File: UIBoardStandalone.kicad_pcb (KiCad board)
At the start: 2 copper layers, 132 x 68.5 mm, 49 parts, among them J10 Conn_02x15_Odd_Even, J17 Conn_02x08_Odd_Even, SW1 Button_X, SW10 Button_6, SW11 Button_S, SW12 Button_7, SW13 Button_8, SW14 Button_9, SW15 Button_G, SW16 Button_Y, SW17 Button_0, SW18 Button_Z, SW2 Button_R, SW3 Button_1, SW4 Button_2, SW5 Button_3, SW6 Button_P, SW7 Button_M, SW8 Button_4, SW9 Button_5, U1 HD1077R, U10 MM74C923, U11 HD1077R, U12 HD1077R, U13 HD1077R, U14 HD1077R, U15 HD1077R, U16 HD1077R, U17 HD1077R, U2 HD1077R, U3 HD1077R, U4 HD1077R, U5 HD1077R, U6 HD1077R, U7 HD1077R, U8 HD1077R, U9 HD1077R

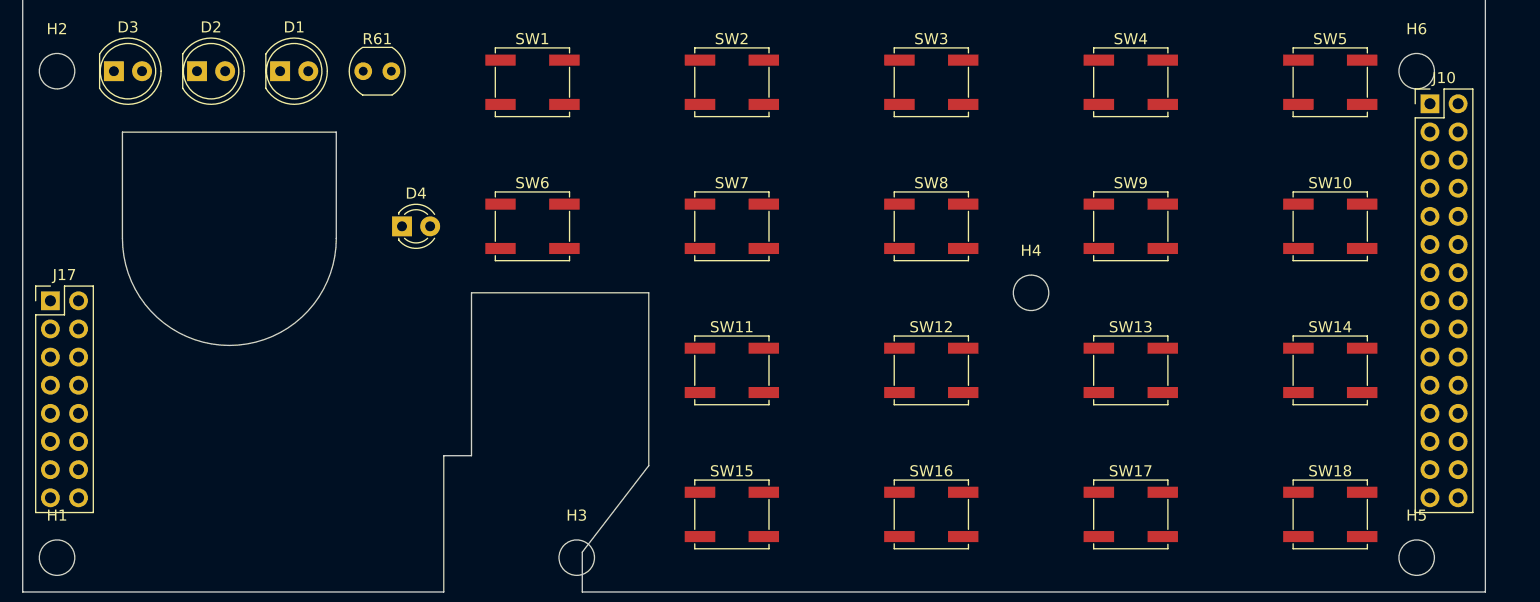
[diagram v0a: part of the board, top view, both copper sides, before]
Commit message: - Steckverbinder auf Rueckseite gespiegelt
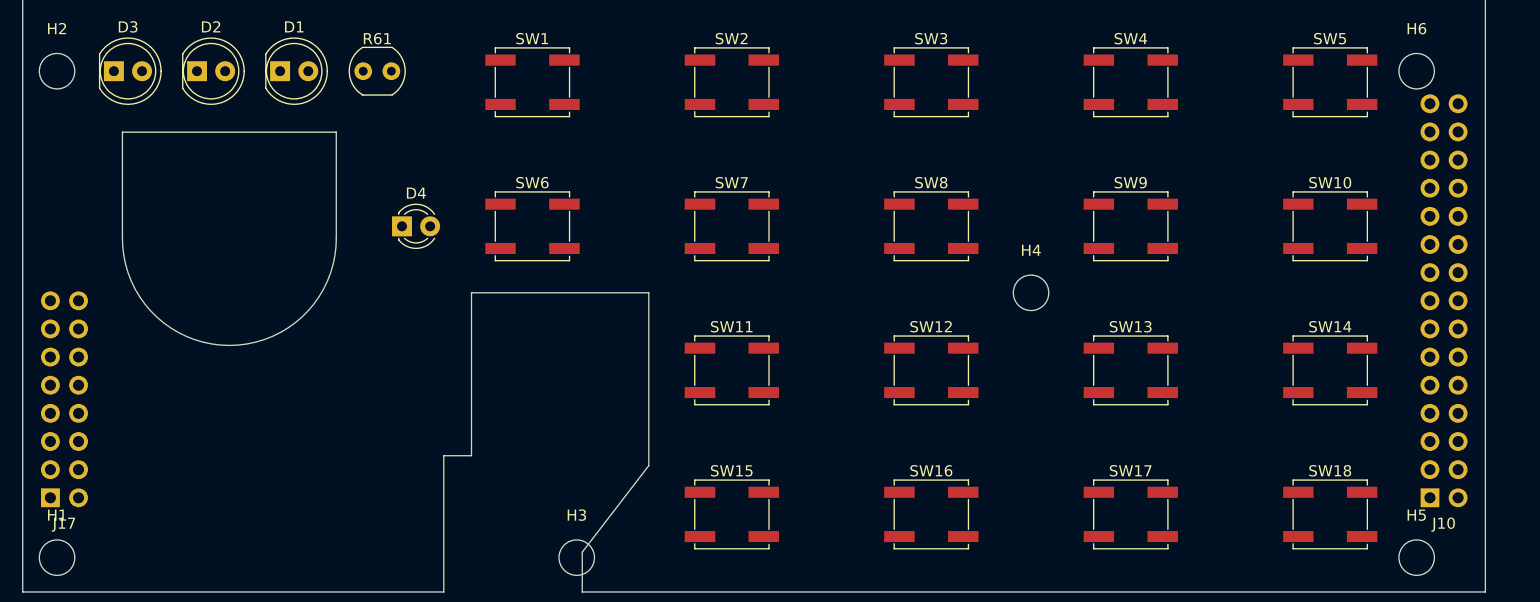
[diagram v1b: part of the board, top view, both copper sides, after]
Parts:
- J10, J17: moved to B.Cu
- moved J10 35.6 mm to (127.0, 60.0)
- moved J17 17.8 mm to (2.50, 60.0)

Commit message: - Outline / Postionierung Zwischenstand
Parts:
- moved U2 125.4 mm to (92.6, 69.0)
- moved U3 125.2 mm to (100.2, 69.0)
- moved U4 124.9 mm to (107.9, 69.0)
- moved U5 124.7 mm to (115.5, 69.0)
- moved U6 124.4 mm to (123.1, 69.0)
- moved U7 124.2 mm to (130.7, 69.0)
- moved U8 123.9 mm to (138.3, 69.0)
- moved U9 123.7 mm to (146.0, 69.0)
- moved U10 123.4 mm to (153.6, 69.0)
- moved U11 123.2 mm to (161.2, 69.0)
- moved U12 122.9 mm to (168.8, 69.0)
- moved U13 122.7 mm to (176.4, 69.0)
- moved U14 122.4 mm to (184.1, 69.0)
- moved U15 122.2 mm to (191.7, 69.0)
- moved H5 100.0 mm to (207.5, 123.0)
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- renumbered J17 to J1, J10 to J2, R61 to R1, U11 to U10, U12 to U11, U13 to U12, U14 to U13, U15 to U14, U16 to U15, U17 to U16, U10 to U17

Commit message: - erster Stand für Abmessungen
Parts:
- D1: value LED_RED -> LED_RD
- D2: value LED_YELLOW -> LED_YL
- D3: value LED_GREEN -> LED_GN
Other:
- board text added: "Ø3,2"
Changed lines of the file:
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@@
   (general
     (thickness 1.6)
-    (drawings 60)
+    (drawings 66)
     (tracks 0)
     (zones 0)
@@
       (effects (font (size 1 1) (thickness 0.15)))
     )
-    (fp_text value LED_GREEN (at 5.5 0 180) (layer F.Fab)
+    (fp_text value LED_GN (at 5.5 0 180) (layer F.Fab)
       (effects (font (size 1 1) (thickness 0.15)))
     )
@@
       (effects (font (size 1 1) (thickness 0.15)))
     )
-    (fp_text value LED_YELLOW (at 5.5 0 180) (layer F.Fab)
+    (fp_text value LED_YL (at 5.5 0 180) (layer F.Fab)
       (effects (font (size 1 1) (thickness 0.15)))
     )
@@
       (effects (font (size 1 1) (thickness 0.15)))
     )
-    (fp_text value LED_RED (at 5.5 0 180) (layer F.Fab)
+    (fp_text value LED_RD (at 5.5 0 180) (layer F.Fab)
       (effects (font (size 1 1) (thickness 0.15)))
     )
@@
     )
   )
+  (gr_text Ø3,2 (at 86 73.5) (layer Dwgs.User)
+    (effects (font (size 1 1) (thickness 0.15)))
+  )
+  (gr_text Ø3,2 (at 169.5 95) (layer Dwgs.User)
+    (effects (font (size 1 1) (thickness 0.15)))
+  )
+  (gr_text Ø3,2 (at 203 73.5) (layer Dwgs.User)
+    (effects (font (size 1 1) (thickness 0.15)))
+  )
+  (gr_text Ø3,2 (at 203 120.5) (layer Dwgs.User)
+    (effects (font (size 1 1) (thickness 0.15)))
+  )
+  (gr_text Ø3,2 (at 129 119) (layer Dwgs.User)
+    (effects (font (size 1 1) (thickness 0.15)))
+  )
+  (gr_text Ø3,2 (at 86 120.5) (layer Dwgs.User)
+    (effects (font (size 1 1) (thickness 0.15)))
+  )
   (dimension 3 (width 0.15) (layer Dwgs.User)
     (gr_text "3,0 mm" (at 74.2 124.5 90) (layer Dwgs.User)
@@
   )
   (dimension 53.000094 (width 0.15) (layer Dwgs.User)
-    (gr_text "53,000 mm" (at 105.042264 145.349995 0.1081051161) (layer Dwgs.User)
-      (effects (font (size 1 1) (thickness 0.15)))
-    )
-    (feature1 (pts (xy 78.5 123) (xy 78.540918 144.686417)))
-    (feature2 (pts (xy 131.5 122.9) (xy 131.540918 144.586417)))
-    (crossbar (pts (xy 131.539811 143.999997) (xy 78.539811 144.099997)))
-    (arrow1a (pts (xy 78.539811 144.099997) (xy 79.665206 143.511452)))
-    (arrow1b (pts (xy 78.539811 144.099997) (xy 79.667419 144.684291)))
-    (arrow2a (pts (xy 131.539811 143.999997) (xy 130.412203 143.415703)))
-    (arrow2b (pts (xy 131.539811 143.999997) (xy 130.414416 144.588542)))
+    (gr_text "53,000 mm" (at 105.042264 145.349994 0.1081051161) (layer Dwgs.User)
+      (effects (font (size 1 1) (thickness 0.15)))
+    )
+    (feature1 (pts (xy 78.5 123) (xy 78.540918 144.686416)))
+    (feature2 (pts (xy 131.5 122.9) (xy 131.540918 144.586416)))
+    (crossbar (pts (xy 131.539811 143.999996) (xy 78.539811 144.099996)))
+    (arrow1a (pts (xy 78.539811 144.099996) (xy 79.665206 143.511451)))
+    (arrow1b (pts (xy 78.539811 144.099996) (xy 79.667419 144.68429)))
+    (arrow2a (pts (xy 131.539811 143.999996) (xy 130.412203 143.415702)))
+    (arrow2b (pts (xy 131.539811 143.999996) (xy 130.414416 144.588541)))
   )
   (dimension 114.3 (width 0.15) (layer Dwgs.User)

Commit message: [fix:] measurement errors [add:] backlight LEDs
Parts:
- added D5: LED_BL1, LED_THT:LED_D3.0mm, F.Cu at (115.5, 87.3)
- added D6: LED_BL2, LED_THT:LED_D3.0mm, F.Cu at (151.5, 87.3)
- added D7: LED_BL3, LED_THT:LED_D3.0mm, F.Cu at (187.5, 87.3)
- added D8: LED_BL4, LED_THT:LED_D3.0mm, F.Cu at (151.5, 113.8)
- added D9: LED_BL5, LED_THT:LED_D3.0mm, F.Cu at (187.5, 113.8)
- moved D1 1.00 mm to (102.8, 81.3)
- moved D2 1.00 mm to (95.3, 81.3)
- moved D3 1.00 mm to (87.8, 81.3)
- moved R1 1.00 mm to (110.3, 81.3)
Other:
- outline, holes or cut-outs redrawn

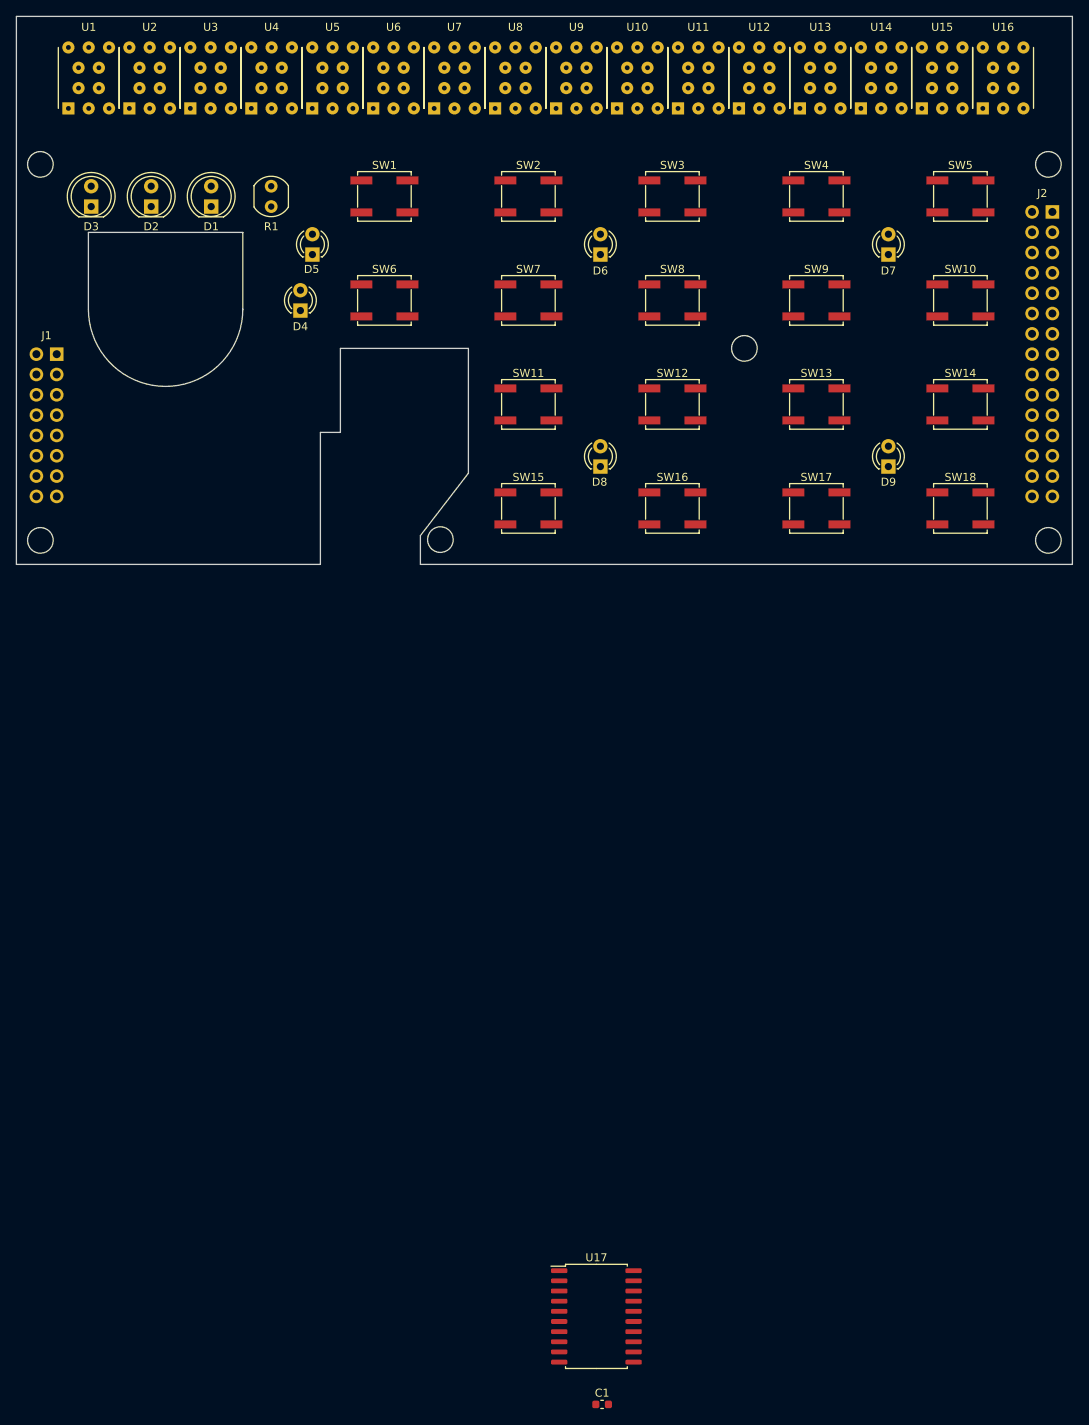
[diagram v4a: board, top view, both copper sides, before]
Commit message: - Erster Stand UI Board Layout
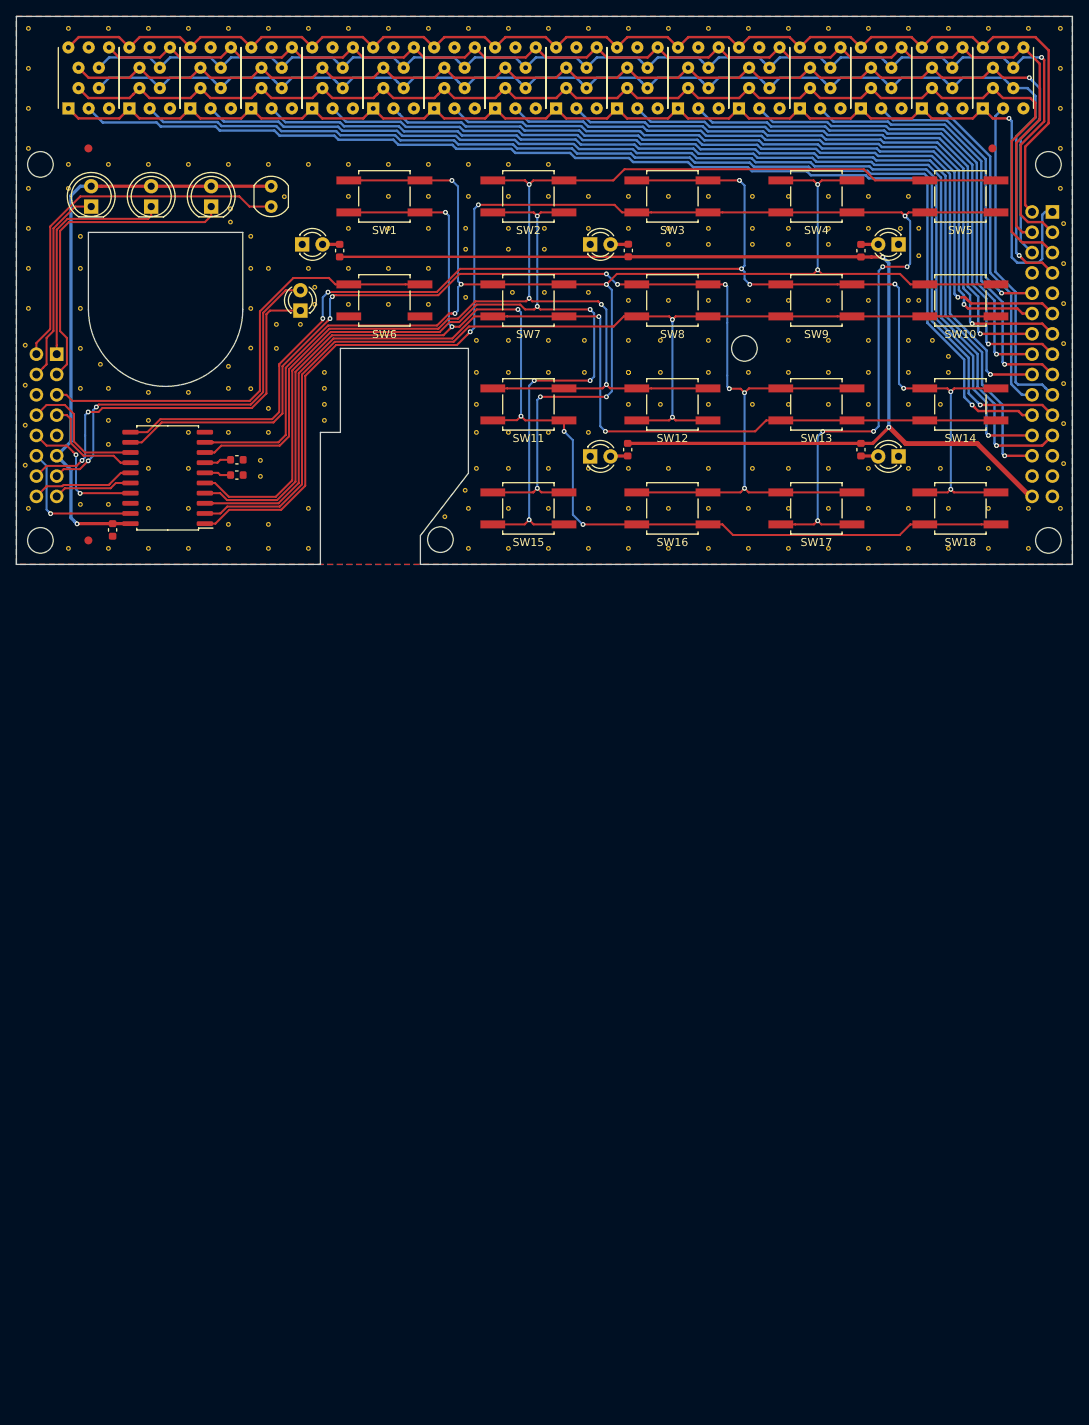
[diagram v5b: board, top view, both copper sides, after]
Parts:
- added C2: 2u2/10V/X5R, Capacitor_SMD:C_0603_1608Metric, F.Cu at (106.1, 112.9)
- added C3: 220n/10V/X5R, Capacitor_SMD:C_0603_1608Metric, F.Cu at (106.1, 114.8)
- added R2: tbd, Resistor_SMD:R_0603_1608Metric, F.Cu at (118.9, 86.8)
- added R3: tbd, Resistor_SMD:R_0603_1608Metric, F.Cu at (155.0, 86.8)
- added R4: tbd, Resistor_SMD:R_0603_1608Metric, F.Cu at (184.1, 86.8)
- added R5: tbd, Resistor_SMD:R_0603_1608Metric, F.Cu at (154.9, 111.7)
- added R6: tbd, Resistor_SMD:R_0603_1608Metric, F.Cu at (184.1, 111.7)
- added REF**: VIA_0.6mm, TeKaDe:VIA_0.6mm, F.Cu at (134.7, 84.0)
- added REF**: VIA_0.6mm, TeKaDe:VIA_0.6mm, F.Cu at (100.0, 76.0)
- added REF**: VIA_0.6mm, TeKaDe:VIA_0.6mm, F.Cu at (85.0, 76.0)
- added REF**: VIA_0.6mm, TeKaDe:VIA_0.6mm, F.Cu at (190.0, 80.0)
- added REF**: VIA_0.6mm, TeKaDe:VIA_0.6mm, F.Cu at (185.0, 80.0)
- added REF**: VIA_0.6mm, TeKaDe:VIA_0.6mm, F.Cu at (180.0, 80.0)
- added REF**: VIA_0.6mm, TeKaDe:VIA_0.6mm, F.Cu at (175.0, 80.0)
- added REF**: VIA_0.6mm, TeKaDe:VIA_0.6mm, F.Cu at (170.5, 80.0)
- added REF**: VIA_0.6mm, TeKaDe:VIA_0.6mm, F.Cu at (165.0, 80.0)
- added REF**: VIA_0.6mm, TeKaDe:VIA_0.6mm, F.Cu at (160.0, 80.0)
- added REF**: VIA_0.6mm, TeKaDe:VIA_0.6mm, F.Cu at (155.0, 80.0)
- added REF**: VIA_0.6mm, TeKaDe:VIA_0.6mm, F.Cu at (150.0, 80.0)
- added REF**: VIA_0.6mm, TeKaDe:VIA_0.6mm, F.Cu at (105.0, 76.0)
- added REF**: VIA_0.6mm, TeKaDe:VIA_0.6mm, F.Cu at (145.0, 80.0)
- added REF**: VIA_0.6mm, TeKaDe:VIA_0.6mm, F.Cu at (140.0, 80.0)
- added REF**: VIA_0.6mm, TeKaDe:VIA_0.6mm, F.Cu at (135.0, 80.0)
- added REF**: VIA_0.6mm, TeKaDe:VIA_0.6mm, F.Cu at (130.0, 80.0)
- added REF**: VIA_0.6mm, TeKaDe:VIA_0.6mm, F.Cu at (125.0, 80.0)
- added REF**: VIA_0.6mm, TeKaDe:VIA_0.6mm, F.Cu at (120.0, 80.0)
- added REF**: VIA_0.6mm, TeKaDe:VIA_0.6mm, F.Cu at (85.0, 79.0)
- added REF**: VIA_0.6mm, TeKaDe:VIA_0.6mm, F.Cu at (189.0, 84.0)
- added REF**: VIA_0.6mm, TeKaDe:VIA_0.6mm, F.Cu at (185.0, 84.0)
- added REF**: VIA_0.6mm, TeKaDe:VIA_0.6mm, F.Cu at (180.0, 84.0)
- added REF**: VIA_0.6mm, TeKaDe:VIA_0.6mm, F.Cu at (110.0, 76.0)
- added REF**: VIA_0.6mm, TeKaDe:VIA_0.6mm, F.Cu at (175.0, 84.0)
- added REF**: VIA_0.6mm, TeKaDe:VIA_0.6mm, F.Cu at (170.5, 84.0)
- added REF**: VIA_0.6mm, TeKaDe:VIA_0.6mm, F.Cu at (165.0, 84.0)
- added REF**: VIA_0.6mm, TeKaDe:VIA_0.6mm, F.Cu at (160.0, 84.0)
- added REF**: VIA_0.6mm, TeKaDe:VIA_0.6mm, F.Cu at (155.0, 84.0)
- added REF**: VIA_0.6mm, TeKaDe:VIA_0.6mm, F.Cu at (150.0, 84.0)
- added REF**: VIA_0.6mm, TeKaDe:VIA_0.6mm, F.Cu at (144.5, 84.0)
- added REF**: VIA_0.6mm, TeKaDe:VIA_0.6mm, F.Cu at (140.0, 84.0)
- added REF**: VIA_0.6mm, TeKaDe:VIA_0.6mm, F.Cu at (130.0, 84.0)
- added REF**: VIA_0.6mm, TeKaDe:VIA_0.6mm, F.Cu at (125.0, 84.0)
- added REF**: VIA_0.6mm, TeKaDe:VIA_0.6mm, F.Cu at (115.0, 76.0)
- added REF**: VIA_0.6mm, TeKaDe:VIA_0.6mm, F.Cu at (120.0, 84.0)
- added REF**: VIA_0.6mm, TeKaDe:VIA_0.6mm, F.Cu at (86.5, 85.0)
- added REF**: VIA_0.6mm, TeKaDe:VIA_0.6mm, F.Cu at (180.0, 86.0)
- added REF**: VIA_0.6mm, TeKaDe:VIA_0.6mm, F.Cu at (175.0, 86.0)
- added REF**: VIA_0.6mm, TeKaDe:VIA_0.6mm, F.Cu at (170.5, 86.0)
- added REF**: VIA_0.6mm, TeKaDe:VIA_0.6mm, F.Cu at (165.0, 86.0)
- added REF**: VIA_0.6mm, TeKaDe:VIA_0.6mm, F.Cu at (160.0, 86.0)
- added REF**: VIA_0.6mm, TeKaDe:VIA_0.6mm, F.Cu at (144.5, 86.6)
- added REF**: VIA_0.6mm, TeKaDe:VIA_0.6mm, F.Cu at (140.0, 86.6)
- added REF**: VIA_0.6mm, TeKaDe:VIA_0.6mm, F.Cu at (130.0, 89.0)
- added REF**: VIA_0.6mm, TeKaDe:VIA_0.6mm, F.Cu at (112.0, 80.0)
- added REF**: VIA_0.6mm, TeKaDe:VIA_0.6mm, F.Cu at (125.0, 89.0)
- added REF**: VIA_0.6mm, TeKaDe:VIA_0.6mm, F.Cu at (120.0, 89.0)
- added REF**: VIA_0.6mm, TeKaDe:VIA_0.6mm, F.Cu at (115.0, 89.0)
- added REF**: VIA_0.6mm, TeKaDe:VIA_0.6mm, F.Cu at (110.0, 89.0)
- added REF**: VIA_0.6mm, TeKaDe:VIA_0.6mm, F.Cu at (86.5, 89.0)
- added REF**: VIA_0.6mm, TeKaDe:VIA_0.6mm, F.Cu at (190.0, 93.0)
- added REF**: VIA_0.6mm, TeKaDe:VIA_0.6mm, F.Cu at (185.0, 93.0)
- added REF**: VIA_0.6mm, TeKaDe:VIA_0.6mm, F.Cu at (180.0, 93.0)
- added REF**: VIA_0.6mm, TeKaDe:VIA_0.6mm, F.Cu at (175.0, 93.0)
- added REF**: VIA_0.6mm, TeKaDe:VIA_0.6mm, F.Cu at (170.0, 93.0)
- added REF**: VIA_0.6mm, TeKaDe:VIA_0.6mm, F.Cu at (105.3, 83.2)
- added REF**: VIA_0.6mm, TeKaDe:VIA_0.6mm, F.Cu at (165.0, 93.0)
- added REF**: VIA_0.6mm, TeKaDe:VIA_0.6mm, F.Cu at (160.0, 93.0)
- added REF**: VIA_0.6mm, TeKaDe:VIA_0.6mm, F.Cu at (155.0, 93.0)
- added REF**: VIA_0.6mm, TeKaDe:VIA_0.6mm, F.Cu at (150.0, 92.0)
- added REF**: VIA_0.6mm, TeKaDe:VIA_0.6mm, F.Cu at (140.5, 92.0)
- added REF**: VIA_0.6mm, TeKaDe:VIA_0.6mm, F.Cu at (130.0, 93.5)
- added REF**: VIA_0.6mm, TeKaDe:VIA_0.6mm, F.Cu at (125.0, 93.5)
- added REF**: VIA_0.6mm, TeKaDe:VIA_0.6mm, F.Cu at (120.0, 93.5)
- added REF**: VIA_0.6mm, TeKaDe:VIA_0.6mm, F.Cu at (115.8, 93.5)
- added REF**: VIA_0.6mm, TeKaDe:VIA_0.6mm, F.Cu at (86.5, 94.0)
- added REF**: VIA_0.6mm, TeKaDe:VIA_0.6mm, F.Cu at (105.3, 81.6)
- added REF**: VIA_0.6mm, TeKaDe:VIA_0.6mm, F.Cu at (195.0, 100.0)
- added REF**: VIA_0.6mm, TeKaDe:VIA_0.6mm, F.Cu at (190.0, 98.0)
- added REF**: VIA_0.6mm, TeKaDe:VIA_0.6mm, F.Cu at (185.0, 98.0)
- added REF**: VIA_0.6mm, TeKaDe:VIA_0.6mm, F.Cu at (180.0, 98.0)
- added REF**: VIA_0.6mm, TeKaDe:VIA_0.6mm, F.Cu at (175.0, 98.0)
- added REF**: VIA_0.6mm, TeKaDe:VIA_0.6mm, F.Cu at (165.0, 98.0)
- added REF**: VIA_0.6mm, TeKaDe:VIA_0.6mm, F.Cu at (159.0, 98.0)
- added REF**: VIA_0.6mm, TeKaDe:VIA_0.6mm, F.Cu at (155.0, 98.0)
- added REF**: VIA_0.6mm, TeKaDe:VIA_0.6mm, F.Cu at (149.5, 98.0)
- added REF**: VIA_0.6mm, TeKaDe:VIA_0.6mm, F.Cu at (145.0, 98.0)
- added REF**: VIA_0.6mm, TeKaDe:VIA_0.6mm, F.Cu at (107.8, 85.0)
- added REF**: VIA_0.6mm, TeKaDe:VIA_0.6mm, F.Cu at (140.0, 98.0)
- added REF**: VIA_0.6mm, TeKaDe:VIA_0.6mm, F.Cu at (111.0, 96.0)
- added REF**: VIA_0.6mm, TeKaDe:VIA_0.6mm, F.Cu at (111.0, 99.0)
- added REF**: VIA_0.6mm, TeKaDe:VIA_0.6mm, F.Cu at (86.5, 99.0)
- added REF**: VIA_0.6mm, TeKaDe:VIA_0.6mm, F.Cu at (195.0, 102.0)
- added REF**: VIA_0.6mm, TeKaDe:VIA_0.6mm, F.Cu at (190.0, 102.0)
- added REF**: VIA_0.6mm, TeKaDe:VIA_0.6mm, F.Cu at (185.0, 102.0)
- added REF**: VIA_0.6mm, TeKaDe:VIA_0.6mm, F.Cu at (180.0, 102.0)
- added REF**: VIA_0.6mm, TeKaDe:VIA_0.6mm, F.Cu at (175.0, 102.0)
- added REF**: VIA_0.6mm, TeKaDe:VIA_0.6mm, F.Cu at (170.0, 102.0)
- added REF**: VIA_0.6mm, TeKaDe:VIA_0.6mm, F.Cu at (107.8, 89.0)
- added REF**: VIA_0.6mm, TeKaDe:VIA_0.6mm, F.Cu at (165.0, 102.0)
- added REF**: VIA_0.6mm, TeKaDe:VIA_0.6mm, F.Cu at (159.0, 102.0)
- added REF** (x2): VIA_0.6mm, TeKaDe:VIA_0.6mm, F.Cu at (155.0, 102.0)
- added REF**: VIA_0.6mm, TeKaDe:VIA_0.6mm, F.Cu at (149.5, 102.0)
- added REF**: VIA_0.6mm, TeKaDe:VIA_0.6mm, F.Cu at (145.0, 102.0)
- added REF**: VIA_0.6mm, TeKaDe:VIA_0.6mm, F.Cu at (140.0, 102.0)
- added REF**: VIA_0.6mm, TeKaDe:VIA_0.6mm, F.Cu at (117.0, 104.0)
- added REF**: VIA_0.6mm, TeKaDe:VIA_0.6mm, F.Cu at (110.0, 106.5)
- added REF**: VIA_0.6mm, TeKaDe:VIA_0.6mm, F.Cu at (105.0, 104.0)
- added REF**: VIA_0.6mm, TeKaDe:VIA_0.6mm, F.Cu at (100.0, 104.5)
- added REF**: VIA_0.6mm, TeKaDe:VIA_0.6mm, F.Cu at (107.8, 94.0)
- added REF**: VIA_0.6mm, TeKaDe:VIA_0.6mm, F.Cu at (95.0, 104.5)
- added REF**: VIA_0.6mm, TeKaDe:VIA_0.6mm, F.Cu at (90.0, 104.0)
- added REF**: VIA_0.6mm, TeKaDe:VIA_0.6mm, F.Cu at (86.5, 104.0)
- added REF**: VIA_0.6mm, TeKaDe:VIA_0.6mm, F.Cu at (170.5, 106.0)
- added REF**: VIA_0.6mm, TeKaDe:VIA_0.6mm, F.Cu at (165.0, 106.0)
- added REF**: VIA_0.6mm, TeKaDe:VIA_0.6mm, F.Cu at (159.0, 106.0)
- added REF**: VIA_0.6mm, TeKaDe:VIA_0.6mm, F.Cu at (155.0, 106.0)
- added REF**: VIA_0.6mm, TeKaDe:VIA_0.6mm, F.Cu at (150.0, 109.5)
- added REF**: VIA_0.6mm, TeKaDe:VIA_0.6mm, F.Cu at (145.0, 109.5)
- added REF**: VIA_0.6mm, TeKaDe:VIA_0.6mm, F.Cu at (140.0, 109.5)
- added REF**: VIA_0.6mm, TeKaDe:VIA_0.6mm, F.Cu at (134.7, 86.6)
- added REF**: VIA_0.6mm, TeKaDe:VIA_0.6mm, F.Cu at (107.8, 99.0)
- added REF**: VIA_0.6mm, TeKaDe:VIA_0.6mm, F.Cu at (117.0, 108.0)
- added REF**: VIA_0.6mm, TeKaDe:VIA_0.6mm, F.Cu at (110.0, 109.5)
- added REF**: VIA_0.6mm, TeKaDe:VIA_0.6mm, F.Cu at (105.0, 109.5)
- added REF**: VIA_0.6mm, TeKaDe:VIA_0.6mm, F.Cu at (100.0, 109.5)
- added REF**: VIA_0.6mm, TeKaDe:VIA_0.6mm, F.Cu at (95.0, 108.0)
- added REF**: VIA_0.6mm, TeKaDe:VIA_0.6mm, F.Cu at (90.0, 108.0)
- added REF**: VIA_0.6mm, TeKaDe:VIA_0.6mm, F.Cu at (200.0, 114.0)
- added REF**: VIA_0.6mm, TeKaDe:VIA_0.6mm, F.Cu at (194.0, 114.0)
- added REF**: VIA_0.6mm, TeKaDe:VIA_0.6mm, F.Cu at (190.0, 114.0)
- added REF**: VIA_0.6mm, TeKaDe:VIA_0.6mm, F.Cu at (185.0, 114.0)
- added REF**: VIA_0.6mm, TeKaDe:VIA_0.6mm, F.Cu at (107.8, 104.0)
- added REF**: VIA_0.6mm, TeKaDe:VIA_0.6mm, F.Cu at (180.0, 114.0)
- added REF**: VIA_0.6mm, TeKaDe:VIA_0.6mm, F.Cu at (175.0, 114.0)
- added REF**: VIA_0.6mm, TeKaDe:VIA_0.6mm, F.Cu at (170.5, 114.0)
- added REF**: VIA_0.6mm, TeKaDe:VIA_0.6mm, F.Cu at (165.0, 114.0)
- added REF**: VIA_0.6mm, TeKaDe:VIA_0.6mm, F.Cu at (160.0, 114.0)
- added REF**: VIA_0.6mm, TeKaDe:VIA_0.6mm, F.Cu at (155.0, 114.0)
- added REF**: VIA_0.6mm, TeKaDe:VIA_0.6mm, F.Cu at (150.0, 114.0)
- added REF**: VIA_0.6mm, TeKaDe:VIA_0.6mm, F.Cu at (145.0, 114.0)
- added REF**: VIA_0.6mm, TeKaDe:VIA_0.6mm, F.Cu at (140.0, 114.0)
- added REF**: VIA_0.6mm, TeKaDe:VIA_0.6mm, F.Cu at (117.0, 102.0)
- added REF**: VIA_0.6mm, TeKaDe:VIA_0.6mm, F.Cu at (89.0, 101.0)
- added REF**: VIA_0.6mm, TeKaDe:VIA_0.6mm, F.Cu at (109.0, 115.0)
- added REF**: VIA_0.6mm, TeKaDe:VIA_0.6mm, F.Cu at (109.0, 113.0)
- added REF**: VIA_0.6mm, TeKaDe:VIA_0.6mm, F.Cu at (100.0, 114.0)
- added REF**: VIA_0.6mm, TeKaDe:VIA_0.6mm, F.Cu at (95.0, 114.0)
- added REF**: VIA_0.6mm, TeKaDe:VIA_0.6mm, F.Cu at (205.0, 119.0)
- added REF**: VIA_0.6mm, TeKaDe:VIA_0.6mm, F.Cu at (200.0, 119.0)
- added REF**: VIA_0.6mm, TeKaDe:VIA_0.6mm, F.Cu at (195.0, 119.0)
- added REF**: VIA_0.6mm, TeKaDe:VIA_0.6mm, F.Cu at (190.0, 119.0)
- added REF**: VIA_0.6mm, TeKaDe:VIA_0.6mm, F.Cu at (185.0, 119.0)
- added REF**: VIA_0.6mm, TeKaDe:VIA_0.6mm, F.Cu at (180.0, 119.0)
- added REF**: VIA_0.6mm, TeKaDe:VIA_0.6mm, F.Cu at (105.0, 101.2)
- added REF**: VIA_0.6mm, TeKaDe:VIA_0.6mm, F.Cu at (175.0, 119.0)
- added REF**: VIA_0.6mm, TeKaDe:VIA_0.6mm, F.Cu at (170.0, 119.0)
- added REF**: VIA_0.6mm, TeKaDe:VIA_0.6mm, F.Cu at (165.0, 119.0)
- added REF**: VIA_0.6mm, TeKaDe:VIA_0.6mm, F.Cu at (160.0, 119.0)
- added REF**: VIA_0.6mm, TeKaDe:VIA_0.6mm, F.Cu at (155.0, 119.0)
- added REF**: VIA_0.6mm, TeKaDe:VIA_0.6mm, F.Cu at (150.0, 119.0)
- added REF**: VIA_0.6mm, TeKaDe:VIA_0.6mm, F.Cu at (145.0, 119.0)
- added REF**: VIA_0.6mm, TeKaDe:VIA_0.6mm, F.Cu at (140.0, 119.0)
- added REF**: VIA_0.6mm, TeKaDe:VIA_0.6mm, F.Cu at (135.0, 119.0)
- added REF**: VIA_0.6mm, TeKaDe:VIA_0.6mm, F.Cu at (115.0, 119.0)
- added REF**: VIA_0.6mm, TeKaDe:VIA_0.6mm, F.Cu at (132.1, 120.0)
- added REF**: VIA_0.6mm, TeKaDe:VIA_0.6mm, F.Cu at (110.0, 121.0)
- added REF**: VIA_0.6mm, TeKaDe:VIA_0.6mm, F.Cu at (105.0, 121.0)
- added REF**: VIA_0.6mm, TeKaDe:VIA_0.6mm, F.Cu at (100.0, 119.0)
- added REF**: VIA_0.6mm, TeKaDe:VIA_0.6mm, F.Cu at (95.0, 119.0)
- added REF**: VIA_0.6mm, TeKaDe:VIA_0.6mm, F.Cu at (90.0, 118.5)
- added REF**: VIA_0.6mm, TeKaDe:VIA_0.6mm, F.Cu at (205.0, 124.0)
- added REF**: VIA_0.6mm, TeKaDe:VIA_0.6mm, F.Cu at (200.0, 124.0)
- added REF**: VIA_0.6mm, TeKaDe:VIA_0.6mm, F.Cu at (195.0, 124.0)
- added REF**: VIA_0.6mm, TeKaDe:VIA_0.6mm, F.Cu at (190.0, 124.0)
- added REF**: VIA_0.6mm, TeKaDe:VIA_0.6mm, F.Cu at (185.0, 124.0)
- added REF**: VIA_0.6mm, TeKaDe:VIA_0.6mm, F.Cu at (134.6, 116.7)
- added REF**: VIA_0.6mm, TeKaDe:VIA_0.6mm, F.Cu at (180.0, 124.0)
- added REF**: VIA_0.6mm, TeKaDe:VIA_0.6mm, F.Cu at (175.0, 124.0)
- added REF**: VIA_0.6mm, TeKaDe:VIA_0.6mm, F.Cu at (170.0, 124.0)
- added REF**: VIA_0.6mm, TeKaDe:VIA_0.6mm, F.Cu at (165.0, 124.0)
- added REF**: VIA_0.6mm, TeKaDe:VIA_0.6mm, F.Cu at (160.0, 124.0)
- added REF**: VIA_0.6mm, TeKaDe:VIA_0.6mm, F.Cu at (155.0, 124.0)
- added REF**: VIA_0.6mm, TeKaDe:VIA_0.6mm, F.Cu at (150.0, 124.0)
- added REF**: VIA_0.6mm, TeKaDe:VIA_0.6mm, F.Cu at (145.0, 124.0)
- added REF**: VIA_0.6mm, TeKaDe:VIA_0.6mm, F.Cu at (140.0, 124.0)
- added REF**: VIA_0.6mm, TeKaDe:VIA_0.6mm, F.Cu at (135.0, 124.0)
- added REF**: VIA_0.6mm, TeKaDe:VIA_0.6mm, F.Cu at (90.0, 111.0)
- added REF**: VIA_0.6mm, TeKaDe:VIA_0.6mm, F.Cu at (115.0, 124.0)
- added REF**: VIA_0.6mm, TeKaDe:VIA_0.6mm, F.Cu at (110.0, 124.0)
- added REF**: VIA_0.6mm, TeKaDe:VIA_0.6mm, F.Cu at (105.0, 124.0)
- added REF**: VIA_0.6mm, TeKaDe:VIA_0.6mm, F.Cu at (100.0, 124.0)
- added REF**: VIA_0.6mm, TeKaDe:VIA_0.6mm, F.Cu at (95.0, 124.0)
- added REF**: VIA_0.6mm, TeKaDe:VIA_0.6mm, F.Cu at (90.0, 124.0)
- added REF**: VIA_0.6mm, TeKaDe:VIA_0.6mm, F.Cu at (85.0, 124.0)
- added REF**: Fiducial_1mm_Mask2mm, Fiducial:Fiducial_1mm_Mask2mm, F.Cu at (200.5, 74.0)
- added REF**: Fiducial_1mm_Mask2mm, Fiducial:Fiducial_1mm_Mask2mm, F.Cu at (87.5, 123.0)
- added REF**: Fiducial_1mm_Mask2mm, Fiducial:Fiducial_1mm_Mask2mm, F.Cu at (87.5, 74.0)
- added REF**: VIA_0.6mm, TeKaDe:VIA_0.6mm, F.Cu at (86.5, 118.5)
- added REF**: VIA_0.6mm, TeKaDe:VIA_0.6mm, F.Cu at (79.6, 113.6)
- added REF**: VIA_0.6mm, TeKaDe:VIA_0.6mm, F.Cu at (79.6, 108.6)
- added REF**: VIA_0.6mm, TeKaDe:VIA_0.6mm, F.Cu at (134.7, 92.6)
- added REF**: VIA_0.6mm, TeKaDe:VIA_0.6mm, F.Cu at (79.6, 103.6)
- added REF**: VIA_0.6mm, TeKaDe:VIA_0.6mm, F.Cu at (79.6, 98.6)
- added REF**: VIA_0.6mm, TeKaDe:VIA_0.6mm, F.Cu at (209.4, 113.4)
- added REF**: VIA_0.6mm, TeKaDe:VIA_0.6mm, F.Cu at (209.4, 108.4)
- added REF**: VIA_0.6mm, TeKaDe:VIA_0.6mm, F.Cu at (209.0, 119.0)
- added REF**: VIA_0.6mm, TeKaDe:VIA_0.6mm, F.Cu at (209.4, 103.4)
- added REF**: VIA_0.6mm, TeKaDe:VIA_0.6mm, F.Cu at (209.4, 98.4)
- added REF**: VIA_0.6mm, TeKaDe:VIA_0.6mm, F.Cu at (209.4, 93.4)
- added REF**: VIA_0.6mm, TeKaDe:VIA_0.6mm, F.Cu at (209.4, 88.4)
- added REF**: VIA_0.6mm, TeKaDe:VIA_0.6mm, F.Cu at (209.4, 83.4)
- added REF**: VIA_0.6mm, TeKaDe:VIA_0.6mm, F.Cu at (115.8, 91.4)
- added REF**: VIA_0.6mm, TeKaDe:VIA_0.6mm, F.Cu at (209.0, 79.0)
- added REF**: VIA_0.6mm, TeKaDe:VIA_0.6mm, F.Cu at (209.0, 74.0)
- added REF**: VIA_0.6mm, TeKaDe:VIA_0.6mm, F.Cu at (209.0, 69.0)
- added REF**: VIA_0.6mm, TeKaDe:VIA_0.6mm, F.Cu at (209.0, 64.0)
- added REF**: VIA_0.6mm, TeKaDe:VIA_0.6mm, F.Cu at (209.0, 59.0)
- added REF**: VIA_0.6mm, TeKaDe:VIA_0.6mm, F.Cu at (205.0, 59.0)
- added REF**: VIA_0.6mm, TeKaDe:VIA_0.6mm, F.Cu at (200.0, 59.0)
- added REF**: VIA_0.6mm, TeKaDe:VIA_0.6mm, F.Cu at (195.0, 59.0)
- added REF**: VIA_0.6mm, TeKaDe:VIA_0.6mm, F.Cu at (190.0, 59.0)
- added REF**: VIA_0.6mm, TeKaDe:VIA_0.6mm, F.Cu at (185.0, 59.0)
- added REF**: VIA_0.6mm, TeKaDe:VIA_0.6mm, F.Cu at (191.3, 93.0)
- added REF**: VIA_0.6mm, TeKaDe:VIA_0.6mm, F.Cu at (180.0, 59.0)
- added REF**: VIA_0.6mm, TeKaDe:VIA_0.6mm, F.Cu at (175.0, 59.0)
- added REF**: VIA_0.6mm, TeKaDe:VIA_0.6mm, F.Cu at (170.0, 59.0)
- added REF**: VIA_0.6mm, TeKaDe:VIA_0.6mm, F.Cu at (165.0, 59.0)
- added REF**: VIA_0.6mm, TeKaDe:VIA_0.6mm, F.Cu at (160.0, 59.0)
- added REF**: VIA_0.6mm, TeKaDe:VIA_0.6mm, F.Cu at (155.0, 59.0)
- added REF**: VIA_0.6mm, TeKaDe:VIA_0.6mm, F.Cu at (150.0, 59.0)
- added REF**: VIA_0.6mm, TeKaDe:VIA_0.6mm, F.Cu at (145.0, 59.0)
- added REF**: VIA_0.6mm, TeKaDe:VIA_0.6mm, F.Cu at (140.0, 59.0)
- added REF**: VIA_0.6mm, TeKaDe:VIA_0.6mm, F.Cu at (135.0, 59.0)
- added REF**: VIA_0.6mm, TeKaDe:VIA_0.6mm, F.Cu at (191.3, 87.4)
- added REF**: VIA_0.6mm, TeKaDe:VIA_0.6mm, F.Cu at (130.0, 59.0)
- added REF**: VIA_0.6mm, TeKaDe:VIA_0.6mm, F.Cu at (125.0, 59.0)
- added REF**: VIA_0.6mm, TeKaDe:VIA_0.6mm, F.Cu at (120.0, 59.0)
- added REF**: VIA_0.6mm, TeKaDe:VIA_0.6mm, F.Cu at (115.0, 59.0)
- added REF**: VIA_0.6mm, TeKaDe:VIA_0.6mm, F.Cu at (110.0, 59.0)
- added REF**: VIA_0.6mm, TeKaDe:VIA_0.6mm, F.Cu at (105.0, 59.0)
- added REF**: VIA_0.6mm, TeKaDe:VIA_0.6mm, F.Cu at (100.0, 59.0)
- added REF**: VIA_0.6mm, TeKaDe:VIA_0.6mm, F.Cu at (95.0, 59.0)
- added REF**: VIA_0.6mm, TeKaDe:VIA_0.6mm, F.Cu at (90.0, 59.0)
- added REF**: VIA_0.6mm, TeKaDe:VIA_0.6mm, F.Cu at (85.0, 59.0)
- added REF**: VIA_0.6mm, TeKaDe:VIA_0.6mm, F.Cu at (191.3, 84.0)
- added REF**: VIA_0.6mm, TeKaDe:VIA_0.6mm, F.Cu at (80.0, 59.0)
- added REF**: VIA_0.6mm, TeKaDe:VIA_0.6mm, F.Cu at (80.0, 64.0)
- added REF**: VIA_0.6mm, TeKaDe:VIA_0.6mm, F.Cu at (80.0, 69.0)
- added REF**: VIA_0.6mm, TeKaDe:VIA_0.6mm, F.Cu at (80.0, 74.0)
- added REF**: VIA_0.6mm, TeKaDe:VIA_0.6mm, F.Cu at (80.0, 79.0)
- added REF**: VIA_0.6mm, TeKaDe:VIA_0.6mm, F.Cu at (80.0, 84.0)
- added REF**: VIA_0.6mm, TeKaDe:VIA_0.6mm, F.Cu at (80.0, 89.0)
- added REF**: VIA_0.6mm, TeKaDe:VIA_0.6mm, F.Cu at (80.0, 94.0)
- added REF**: VIA_0.6mm, TeKaDe:VIA_0.6mm, F.Cu at (80.0, 119.0)
- added REF**: VIA_0.6mm, TeKaDe:VIA_0.6mm, F.Cu at (114.0, 96.0)
- added REF**: VIA_0.6mm, TeKaDe:VIA_0.6mm, F.Cu at (90.0, 76.0)
- added REF**: VIA_0.6mm, TeKaDe:VIA_0.6mm, F.Cu at (117.0, 106.0)
- added REF**: VIA_0.6mm, TeKaDe:VIA_0.6mm, F.Cu at (193.0, 98.0)
- added REF**: VIA_0.6mm, TeKaDe:VIA_0.6mm, F.Cu at (144.5, 92.0)
- added REF**: VIA_0.6mm, TeKaDe:VIA_0.6mm, F.Cu at (136.0, 98.0)
- added REF**: VIA_0.6mm, TeKaDe:VIA_0.6mm, F.Cu at (136.0, 102.0)
- added REF**: VIA_0.6mm, TeKaDe:VIA_0.6mm, F.Cu at (136.0, 106.0)
- added REF**: VIA_0.6mm, TeKaDe:VIA_0.6mm, F.Cu at (136.0, 109.5)
- added REF**: VIA_0.6mm, TeKaDe:VIA_0.6mm, F.Cu at (136.0, 114.0)
- added REF**: VIA_0.6mm, TeKaDe:VIA_0.6mm, F.Cu at (194.0, 106.0)
- added REF**: VIA_0.6mm, TeKaDe:VIA_0.6mm, F.Cu at (95.0, 76.0)
- added REF**: VIA_0.6mm, TeKaDe:VIA_0.6mm, F.Cu at (190.0, 106.0)
- added REF**: VIA_0.6mm, TeKaDe:VIA_0.6mm, F.Cu at (185.0, 106.0)
- added REF**: VIA_0.6mm, TeKaDe:VIA_0.6mm, F.Cu at (180.0, 106.0)
- added REF**: VIA_0.6mm, TeKaDe:VIA_0.6mm, F.Cu at (175.0, 106.0)
- added REF**: VIA_0.6mm, TeKaDe:VIA_0.6mm, F.Cu at (145.0, 76.0)
- added REF**: VIA_0.6mm, TeKaDe:VIA_0.6mm, F.Cu at (140.0, 76.0)
- added REF**: VIA_0.6mm, TeKaDe:VIA_0.6mm, F.Cu at (135.0, 76.0)
- added REF**: VIA_0.6mm, TeKaDe:VIA_0.6mm, F.Cu at (130.0, 76.0)
- added REF**: VIA_0.6mm, TeKaDe:VIA_0.6mm, F.Cu at (125.0, 76.0)
- added REF**: VIA_0.6mm, TeKaDe:VIA_0.6mm, F.Cu at (120.0, 76.0)
- C1: footprint Resistor_SMD:R_0603_1608Metric -> Capacitor_SMD:C_0603_1608Metric
- SW1, SW10, SW11, SW12, SW13, SW14, SW15, SW16, SW17, SW18, SW2, SW3, SW4, SW5, SW6, SW7, SW8, SW9: footprint Button_Switch_SMD:SW_SPST_EVQP0 -> TeKaDe:SW_Push_CK_KST2x1G
- moved C1 125.3 mm to (90.5, 121.7), turned to 270 degrees
- moved U17 117.7 mm to (97.4, 115.2), turned to 180 degrees
- moved D6 1.80 mm to (150.2, 86.0), turned to 0 degrees
- moved D7 1.80 mm to (188.8, 86.0), turned to 180 degrees
- moved D8 1.80 mm to (150.2, 112.5), turned to 0 degrees
- moved D9 1.80 mm to (188.8, 112.5), turned to 180 degrees
- moved D5 1.80 mm to (114.2, 86.0), turned to 0 degrees
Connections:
- D4 pad 2: +5V -> /OnSwitchLedAnode
- D5 pad 2: +5V -> Net-(D5-Pad2)
- D6 pad 2: +5V -> Net-(D6-Pad2)
- D7 pad 2: +5V -> Net-(D7-Pad2)
- D8 pad 2: +5V -> Net-(D8-Pad2)
- D9 pad 2: +5V -> Net-(D9-Pad2)
- J1 pad 13: +5V -> /OnSwitchLedAnode
- J2 pad 30: +5V -> +5VA
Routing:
- net Net-(SW1-Pad1): track 0.00 -> 207.1 mm, vias 0 -> 9
- net Net-(SW17-Pad2): track 0.00 -> 190.8 mm, vias 0 -> 8
- net Net-(SW14-Pad1): track 0.00 -> 181.7 mm, vias 0 -> 9
- net Net-(SW11-Pad1): track 0.00 -> 179.1 mm, vias 0 -> 4
- net Net-(SW1-Pad2): track 0.00 -> 174.8 mm, vias 0 -> 6
- net /AnodeSegmentE: track 0.00 -> 162.3 mm, vias 0 -> 1
- net /AnodeSegmentF: track 0.00 -> 161.6 mm
- net /AnodeSegmentC: track 0.00 -> 160.4 mm, vias 0 -> 1
- net /AnodeSegmentA: track 0.00 -> 160.4 mm, vias 0 -> 1
- net /AnodeSegmentD: track 0.00 -> 159.3 mm
- net /AnodeSegmentG: track 0.00 -> 158.8 mm, vias 0 -> 1
- net Net-(SW13-Pad1): track 0.00 -> 156.8 mm, vias 0 -> 8
- net /AnodeSegmentB: track 0.00 -> 156.5 mm
- net /CathodeDigit1: track 0.00 -> 147.3 mm, vias 0 -> 1
- net +5VA: track 0.00 -> 144.5 mm, vias 0 -> 2
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- added copper zone on B.Cu, net GND
- added copper zone on F.Cu, net GND
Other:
- net class Cathodes added: clearance 0.254, trace_width 0.3048, via_dia 0.6096, via_drill 0.3048
- net class Default: clearance 0.2 -> 0.1524; trace_width 0.25 -> 0.254; via_dia 0.8 -> 0.6096; via_drill 0.4 -> 0.3048
- rule trace_clearance: 0.2 -> 0.1524
- rule trace_min: 0.2 -> 0.1524
- rule via_min_size: 0.4 -> 0.3048

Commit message: [fix:] LED definition bug
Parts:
- C1: value 100n/10V/X7R -> 100n/16V/X5R
- U17: value MM74C923 -> MM74C923WM

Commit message: - R Values hinzugefügt - Text aktualisiert - vorläufe BOM hinzugefügt
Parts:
- R2, R3, R4, R5, R6: value tbd -> 210R/5%
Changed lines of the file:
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@@
-(kicad_pcb (version 20171130) (host pcbnew "(5.1.10-1-10_14)")
+(kicad_pcb (version 20171130) (host pcbnew "(5.1.5)-3")
   (general
     (thickness 1.6)
@@
       (effects (font (size 1 1) (thickness 0.15)))
     )
-    (fp_text value tbd (at 0 1.43 90) (layer F.Fab)
+    (fp_text value 210R/5% (at 0 1.43 90) (layer F.Fab)
       (effects (font (size 1 1) (thickness 0.15)))
     )
@@
       (effects (font (size 1 1) (thickness 0.15)))
     )
-    (fp_text value tbd (at 0 1.43 90) (layer F.Fab)
+    (fp_text value 210R/5% (at 0 1.43 90) (layer F.Fab)
       (effects (font (size 1 1) (thickness 0.15)))
     )
@@
       (effects (font (size 1 1) (thickness 0.15)))
     )
-    (fp_text value tbd (at 0 1.43 90) (layer F.Fab)
+    (fp_text value 210R/5% (at 0 1.43 90) (layer F.Fab)
       (effects (font (size 1 1) (thickness 0.15)))
     )
@@
       (effects (font (size 1 1) (thickness 0.15)))
     )
-    (fp_text value tbd (at 0 1.43 90) (layer F.Fab)
+    (fp_text value 210R/5% (at 0 1.43 90) (layer F.Fab)
       (effects (font (size 1 1) (thickness 0.15)))
     )
@@
       (effects (font (size 1 1) (thickness 0.15)))
     )
-    (fp_text value tbd (at 0 1.43 90) (layer F.Fab)
+    (fp_text value 210R/5% (at 0 1.43 90) (layer F.Fab)
       (effects (font (size 1 1) (thickness 0.15)))
     )
